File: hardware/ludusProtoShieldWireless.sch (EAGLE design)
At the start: 72 parts, among them Q1 MOSFET-NCHANNELBSS138, Q2 MOSFET-NCHANNELBSS138, U1 ARDUINO, U3 TB6612FNG

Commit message: Updated all issues in SCH.
Also, replaced the switch for the DPDT package.
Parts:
- removed LED1, LED2: Yellow, SparkFun-LED:LED0603
- removed LED3, LED4, LED5: Blue, SparkFun-LED:LED0603
- removed MOD1: XBEE-1XBEE-1_LOCK, SparkFun-RF:XBEE-1XBEE-1_LOCK
- added D4, D6, D8: Blue, SparkFun-LED:LED-BLUE0603
- added D5, D7: Yellow, SparkFun-LED:LED-YELLOW0603
- added U2: ARDUINO, SparkFun-Boards:ARDUINO_R3_SHIELDUNO_R3_SHIELD_NOLABELS_LOCK
- S1, S2: device SparkFun-Electromechanical:SWITCH-SPDTSMD -> SparkFun-Electromechanical:SWITCH-DPDTAYZ0202; VALUE (none) -> DPDT
- U1: value ARDUINO -> XBEE-1XBEE-1_LOCK; device SparkFun-Boards:ARDUINO_R3_SHIELDUNO_R3_SHIELD_NOLABELS_LOCK -> SparkFun-RF:XBEE-1XBEE-1_LOCK
- renumbered LED8 to D2, LED9 to D3
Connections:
- new net D1: LED7.C
- net 3.3V: now also U2.3.3V; no longer U1.3.3V
- net 5V: now also U2.5V; no longer U1.5V
- net A0/SW_RXI: now also U2.A0; no longer U1.A0
- net A1/SW_TXO: now also U2.A1; no longer U1.A1
- net A2: now also U2.A2; no longer U1.A2
- net A3: now also U2.A3; no longer U1.A3
- net A4: now also U2.A4; no longer U1.A4
- net A5: now also U2.A5; no longer U1.A5
- net AIN1: now also U2.D4; no longer U1.D4
- net AIN2: now also U2.*D5; no longer U1.*D5
- net ANALOG_PWR_RAIL: now also S2.2, S2.5; no longer S1.P
- net AOUT2: now also D4.A, D5.C; no longer LED1.C, LED3.A
- net BIN1: now also U2.D7; no longer U1.D7
- net BIN2: now also U2.D8; no longer U1.D8
- net BOUT2: now also D6.A, D7.C; no longer LED2.C, LED4.A
- net D0/RXI: now also U2.RX; no longer U1.RX
- net D1/TXO: now also U2.TX; no longer U1.TX
- net D10: now also U2.*D10; no longer U1.*D10
- net D11: now also U2.*D11; no longer U1.*D11
- net D12: now also U2.D12; no longer U1.D12
- net D13: now also D8.A, U2.D13; no longer LED5.A, U1.D13
- net D2: now also U2.D2; no longer U1.D2
- net D3: now also U2.*D3; no longer U1.*D3
- net DIN: now also U1.DIN; no longer MOD1.DIN
- net DIO0: now also U1.DIO0; no longer MOD1.DIO0
- net DIO1: now also U1.DIO1; no longer MOD1.DIO1
- net DIO11: now also U1.DIO11; no longer MOD1.DIO11
- net DOUT: now also U1.DOUT; no longer LED7.C, MOD1.DOUT
- net FUSED_3.3V: now also U1.VDD; no longer MOD1.VDD
- net FUSED_5V: now also S1.3, S1.6, S2.3, S2.6; no longer S1.S, S2.S
- net FUSED_VIN: now also S1.1, S1.4, S2.1, S2.4; no longer S1.O, S2.O
- net GND: now also U1.GND, U2.GND@0, U2.GND@1, U2.GND@2; no longer MOD1.GND, U1.GND@0, U1.GND@1, U1.GND@2
- net N$1: now also D8.C; no longer LED5.C
- net N$3: now also D5.A; no longer LED1.A
- net N$5: now also D4.C; no longer LED3.C
- net N$8: now also D7.A; no longer LED2.A
- net N$9: now also D6.C; no longer LED4.C
- net PWMA: now also U2.*D6; no longer U1.*D6
- net PWMB: now also U2.*D9; no longer U1.*D9
- net PWR_RAIL: now also S1.2, S1.5; no longer S2.P
- net RESET: now also U2.RES; no longer U1.RES
- net RSSI: now also U1.RSSI; no longer MOD1.RSSI
- net SCL: now also U2.SCL; no longer U1.SCL
- net SDA: now also U2.SDA; no longer U1.SDA
- net VIN: now also U2.VIN; no longer U1.VIN
- net XBEE_RESET: now also U1.RESET; no longer MOD1.RESET
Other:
- note added: "Max Input Voltage:15V Output Current: 1.2A (ave) / 3.2A (peak)"
- note added: "Power Rail Select Switches"
- note removed: "Power Solder Jumpers"
- moved on the sheet: C1, C2, C4, F1, F2, F3, U3

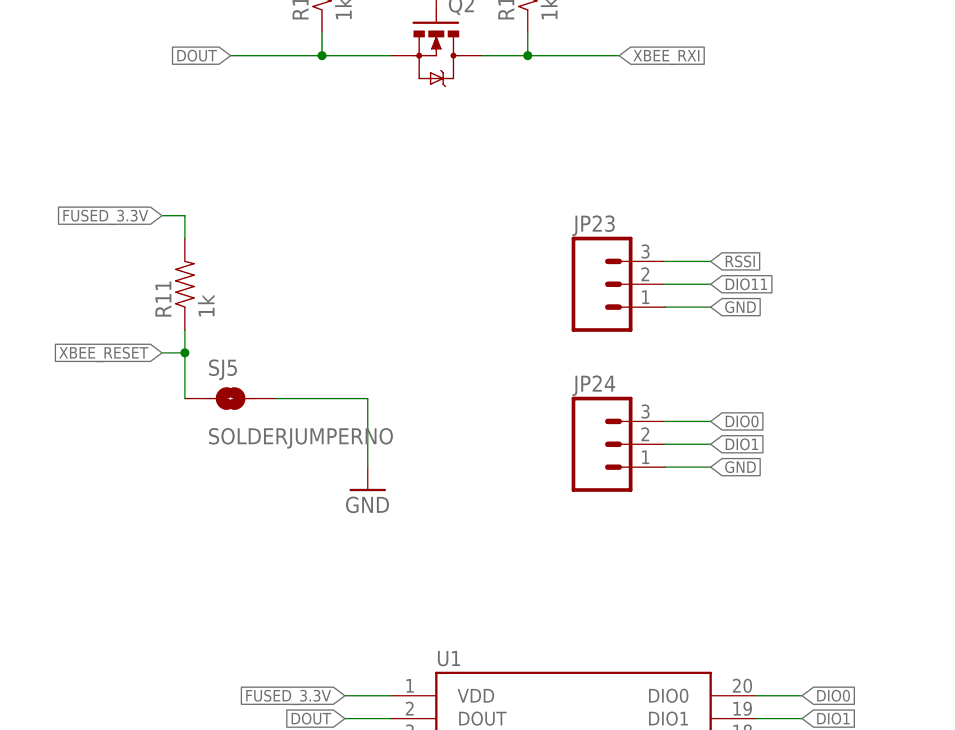
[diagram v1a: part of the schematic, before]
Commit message: Fixed 2 GND flags and SJ5
Updated nets on SJ5 and GND flags
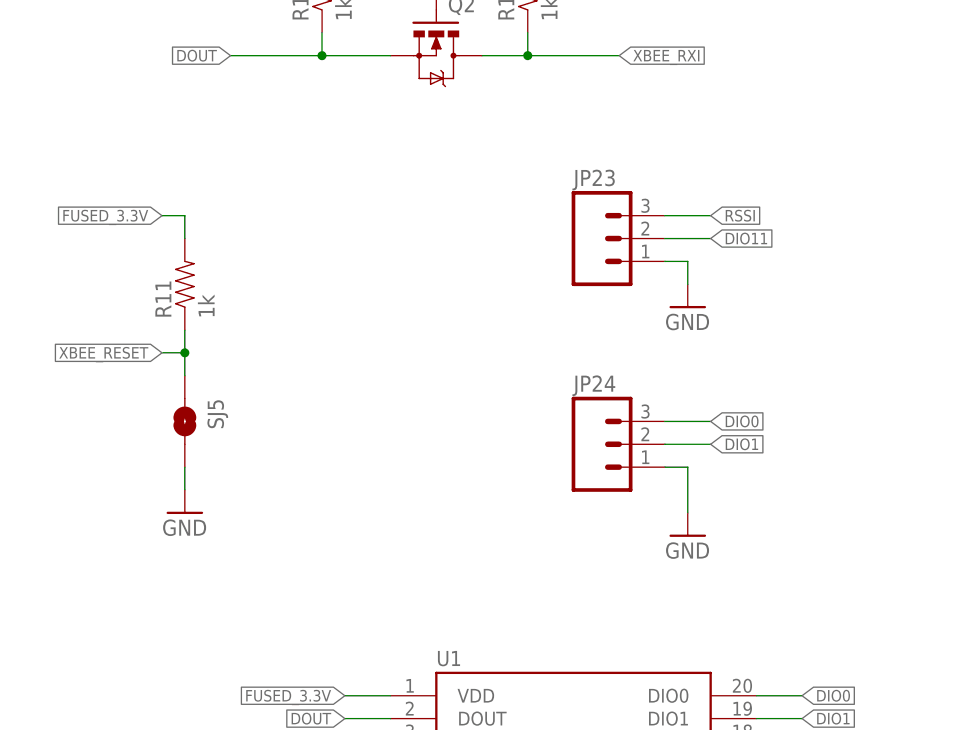
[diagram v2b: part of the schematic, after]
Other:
- moved on the sheet: JP23, SJ5
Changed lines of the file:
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@@
 <setting verticaltext="up"/>
 </settings>
-<grid distance="0.1" unitdist="inch" unit="inch" style="lines" multiple="1" display="yes" altdistance="0.01" altunitdist="inch" altunit="inch"/>
+<grid distance="0.1" unitdist="inch" unit="inch" style="lines" multiple="1" display="no" altdistance="0.01" altunitdist="inch" altunit="inch"/>
 <layers>
 <layer number="1" name="Top" color="4" fill="1" visible="no" active="no"/>
@@
 <part name="R11" library="SparkFun-Resistors" deviceset="1KOHM1/10W1%(0603)" device="" value="1k"/>
 <part name="F3" library="SparkFun-PowerIC" deviceset="PTC" device="SMD" value="PTCSMD"/>
-<part name="SJ5" library="SparkFun-Retired" deviceset="SOLDERJUMPER" device="NO"/>
+<part name="SJ5" library="SparkFun-Retired" deviceset="SOLDERJUMPER" device="NO" value=""/>
 <part name="JP23" library="SparkFun-Connectors" deviceset="M03" device="1X03_NO_SILK"/>
 <part name="JP24" library="SparkFun-Connectors" deviceset="M03" device="1X03_NO_SILK"/>
@@
 <part name="SUPPLY1" library="SparkFun-Aesthetics" deviceset="5V" device=""/>
 <part name="SUPPLY2" library="SparkFun-Aesthetics" deviceset="3.3V" device=""/>
+<part name="GND9" library="SparkFun-Aesthetics" deviceset="GND" device=""/>
+<part name="GND10" library="SparkFun-Aesthetics" deviceset="GND" device=""/>
 </parts>
 <sheets>
@@
 <instance part="FRAME1" gate="G$1" x="0" y="0"/>
 <instance part="FRAME1" gate="G$2" x="330.2" y="0"/>
-<instance part="GND4" gate="1" x="45.72" y="142.24"/>
+<instance part="GND4" gate="1" x="25.4" y="139.7"/>
 <instance part="R11" gate="G$1" x="25.4" y="165.1" rot="R90"/>
 <instance part="F3" gate="G$1" x="294.64" y="256.54"/>
-<instance part="SJ5" gate="1" x="30.48" y="152.4"/>
-<instance part="JP23" gate="G$1" x="71.12" y="165.1"/>
+<instance part="SJ5" gate="1" x="25.4" y="149.86" rot="R270"/>
+<instance part="JP23" gate="G$1" x="71.12" y="170.18"/>
 <instance part="JP24" gate="G$1" x="71.12" y="147.32"/>
 <instance part="U$1" gate="G$1" x="411.48" y="25.4"/>
@@
 <instance part="SUPPLY1" gate="G$1" x="271.78" y="269.24"/>
 <instance part="SUPPLY2" gate="G$1" x="276.86" y="269.24"/>
+<instance part="GND9" gate="1" x="81.28" y="137.16"/>
+<instance part="GND10" gate="1" x="81.28" y="162.56"/>
 </instances>
 <busses>
@@
 </segment>
 <segment>
-<wire x1="35.56" y1="152.4" x2="45.72" y2="152.4" width="0.1524" layer="91"/>
-<wire x1="45.72" y1="152.4" x2="45.72" y2="144.78" width="0.1524" layer="91"/>
+<wire x1="25.4" y1="144.78" x2="25.4" y2="142.24" width="0.1524" layer="91"/>
 <pinref part="GND4" gate="1" pin="GND"/>
 <pinref part="SJ5" gate="1" pin="2"/>
@@
 <segment>
 <pinref part="JP23" gate="G$1" pin="1"/>
-<wire x1="78.74" y1="162.56" x2="83.82" y2="162.56" width="0.1524" layer="91"/>
-<label x="83.82" y="162.56" size="1.27" layer="95" xref="yes"/>
+<wire x1="78.74" y1="167.64" x2="81.28" y2="167.64" width="0.1524" layer="91"/>
+<pinref part="GND10" gate="1" pin="GND"/>
+<wire x1="81.28" y1="165.1" x2="81.28" y2="167.64" width="0.1524" layer="91"/>
 </segment>
 <segment>
 <pinref part="JP24" gate="G$1" pin="1"/>
-<wire x1="78.74" y1="144.78" x2="83.82" y2="144.78" width="0.1524" layer="91"/>
-<label x="83.82" y="144.78" size="1.27" layer="95" xref="yes"/>
+<wire x1="78.74" y1="144.78" x2="81.28" y2="144.78" width="0.1524" layer="91"/>
+<pinref part="GND9" gate="1" pin="GND"/>
+<wire x1="81.28" y1="139.7" x2="81.28" y2="144.78" width="0.1524" layer="91"/>
 </segment>
 </net>
@@
 <segment>
 <pinref part="JP23" gate="G$1" pin="3"/>
-<wire x1="78.74" y1="167.64" x2="83.82" y2="167.64" width="0.1524" layer="91"/>
-<label x="83.82" y="167.64" size="1.27" layer="95" xref="yes"/>
+<wire x1="78.74" y1="172.72" x2="83.82" y2="172.72" width="0.1524" layer="91"/>
+<label x="83.82" y="172.72" size="1.27" layer="95" xref="yes"/>
 </segment>
 </net>
@@
 <wire x1="25.4" y1="160.02" x2="25.4" y2="157.48" width="0.1524" layer="91"/>
 <pinref part="SJ5" gate="1" pin="1"/>
-<wire x1="25.4" y1="152.4" x2="25.4" y2="157.48" width="0.1524" layer="91"/>
+<wire x1="25.4" y1="154.94" x2="25.4" y2="157.48" width="0.1524" layer="91"/>
 <junction x="25.4" y="157.48"/>
 </segment>
@@
 <segment>
 <pinref part="JP23" gate="G$1" pin="2"/>
-<wire x1="78.74" y1="165.1" x2="83.82" y2="165.1" width="0.1524" layer="91"/>
-<label x="83.82" y="165.1" size="1.27" layer="95" xref="yes"/>
-</segment>
-</net>
+<wire x1="78.74" y1="170.18" x2="83.82" y2="170.18" width="0.1524" layer="91"/>
+<label x="83.82" y="170.18" size="1.27" layer="95" xref="yes"/>
+</segment>
+</net>

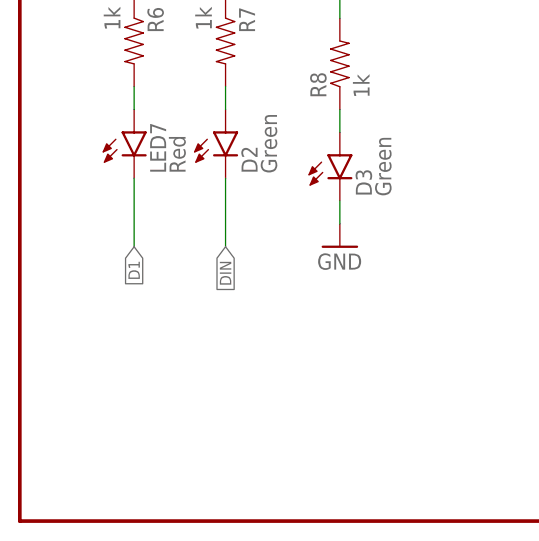
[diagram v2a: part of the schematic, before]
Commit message: Spaced out LEDs / Resistors
Fixed D1 / DOUT break and spaced out LEDs from resistors
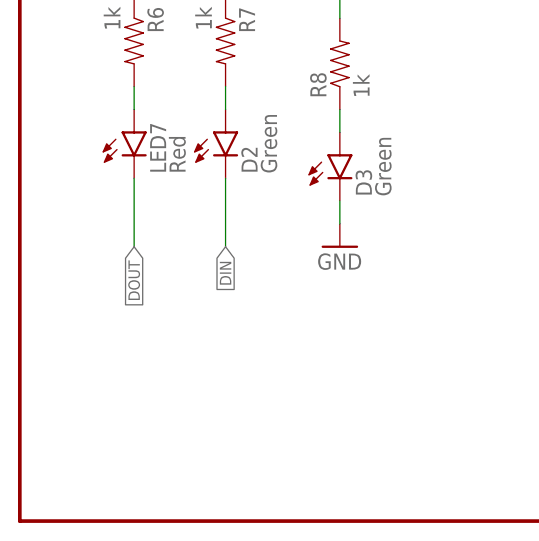
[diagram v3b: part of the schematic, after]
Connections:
- removed net D1: LED7.C
- net DOUT: now also LED7.C
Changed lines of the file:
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@@
 <label x="30.48" y="190.5" size="1.27" layer="95" rot="R180" xref="yes"/>
+</segment>
+<segment>
+<wire x1="12.7" y1="38.1" x2="12.7" y2="30.48" width="0.1524" layer="91"/>
+<label x="12.7" y="30.48" size="1.27" layer="95" rot="R270" xref="yes"/>
+<pinref part="LED7" gate="G$1" pin="C"/>
 </segment>
 </net>
@@
 </segment>
 </net>
-<net name="D1" class="0">
-<segment>
-<wire x1="12.7" y1="38.1" x2="12.7" y2="30.48" width="0.1524" layer="91"/>
-<label x="12.7" y="30.48" size="1.27" layer="95" rot="R270" xref="yes"/>
-<pinref part="LED7" gate="G$1" pin="C"/>
-</segment>
-</net>
